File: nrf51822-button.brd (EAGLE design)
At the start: 22.7 x 20.1 mm, 27 parts, among them U1 nRF51822, X1 16MHz, X2 32.768kHz

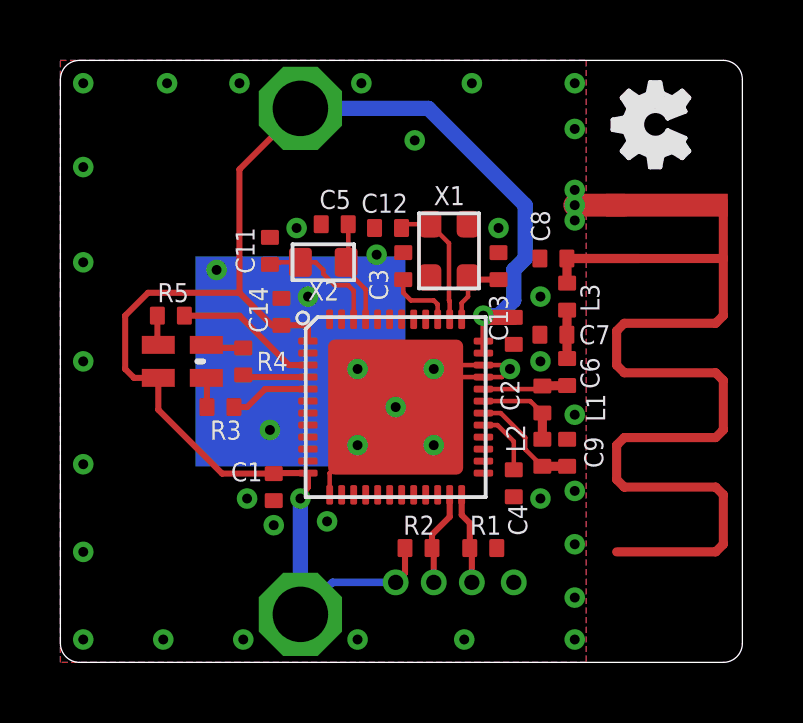
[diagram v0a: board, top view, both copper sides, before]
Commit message: Clean up! This might acutally work (!). Removd 32KHz crystal, added 20 uF of bulk cap for spikes (might need more?). Biggest problem: antenna ok? Do we need the DC-DC converter to reduce the current load on the CR1632 battery? Stay tuned!
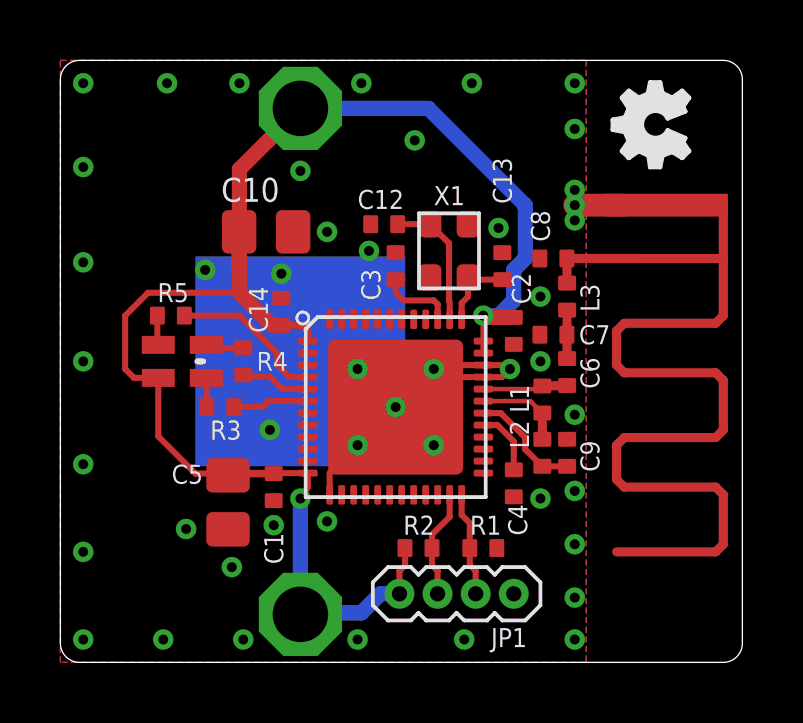
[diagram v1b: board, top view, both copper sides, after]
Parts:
- removed C11: 12pF, rcl_custom:.0402-C-NOSILK
- removed X2: 32.768kHz, AMLib:2P-SMD-2.05X1.2
- added C10: 10u, rcl_custom:.0805-B-NOSILK
- added JP1: (no value), SparkFun-v5:1X04-1.27MM
- C1, C14, C3: value 100nF -> 100n
- C12, C13: value 12pF -> 12p
- C2: value 1nF -> 1n
- C4: value 47nF -> 47n
- C5: value 12pF -> 10u; device rcl_custom:.0402-C-NOSILK -> rcl_custom:.0805-B-NOSILK
- C6: value 2.2pF -> 2.2p
- C7: value 1.0pF -> 1.0p
- C8: value 1.5pF -> 1.5p
- C9: value 2.2nF -> 2.2n
- L1: value 4.7nH -> 4.7n
- L2: value 10nH -> 10n
- L3: value 3.3nH -> 3.3n
- R1, R2: value 12k -> 10k
- U1: value nRF51822 -> NRF51822-QFAB-R7
- moved C5 9.93 mm to (5.59, 5.33), turned to 270 degrees
- moved C3 0.25 mm to (11.2, 13.2)
- moved C12 0.18 mm to (10.8, 14.6)
- moved C13 0.13 mm to (14.7, 13.2)
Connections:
- net ROUTE-ANT renamed ANTENNA
- removed net N$14: C5.2, U1.45, X2.2
- removed net N$16: C11.2, U1.46, X2.1
- net GND: now also C10.2, C5.2, JP1.4; no longer C11.1, C5.1
- net N$1: now also U1.4; no longer U1.3
- net N$2: now also U1.5; no longer U1.4
- net N$3: now also U1.6; no longer U1.5
- net SWDCLK: now also JP1.3
- net SWDIO: now also JP1.2
- net VDD: now also C10.1, C5.1, JP1.1
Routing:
- net N$16: track 4.22 -> 0.00 mm
- net N$14: track 3.47 -> 0.00 mm
- net VDD: track 49.7 -> 51.8 mm, vias 3 -> 2
- net SWDIO: track 3.18 -> 3.62 mm, vias 1 -> 0
- net SWDCLK: track 3.06 -> 3.49 mm, vias 1 -> 0
- net GND: vias 45 -> 46

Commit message: Final board cleanup, including checking values and packages. Routed this one as a prototype on the A406. Also added BOM.
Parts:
- C12, C13: value 12p -> 12p (NPO +- 2%)
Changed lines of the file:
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@@
 <attribute name="VALUE" x="11.184" y="10.378" size="0.635" layer="27" ratio="10" rot="R270"/>
 </element>
-<element name="C12" library="rcl_custom" package=".0402-C-NOSILK" value="12p" x="10.795" y="14.605" smashed="yes" rot="R180">
+<element name="C12" library="rcl_custom" package=".0402-C-NOSILK" value="12p (NPO +- 2%)" x="10.795" y="14.605" smashed="yes" rot="R180">
 <attribute name="NAME" x="9.906" y="15.113" size="0.635" layer="25" font="vector" ratio="20"/>
 <attribute name="VALUE" x="10.033" y="14.351" size="0.4064" layer="27" font="vector" ratio="10"/>
 </element>
-<element name="C13" library="rcl_custom" package=".0402-C-NOSILK" value="12p" x="14.732" y="13.208" smashed="yes" rot="R90">
+<element name="C13" library="rcl_custom" package=".0402-C-NOSILK" value="12p (NPO +- 2%)" x="14.732" y="13.208" smashed="yes" rot="R90">
 <attribute name="NAME" x="14.4145" y="16.8275" size="0.635" layer="25" font="vector" ratio="20" rot="R270"/>
 <attribute name="VALUE" x="14.478" y="13.843" size="0.4064" layer="27" font="vector" ratio="10" rot="R270"/>
